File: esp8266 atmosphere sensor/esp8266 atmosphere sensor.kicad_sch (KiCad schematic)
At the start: 23 parts, among them J1 Conn_02x03_Odd_Even, J2 UJ2-MIBH-G-SMT-TR, J3 LUX sensor, J4 bme280, J5 PIR, J6 Analog in, SW1 SW_MEC_5E, U1 ESP-12F, U2 LD1117S33TR_SOT223

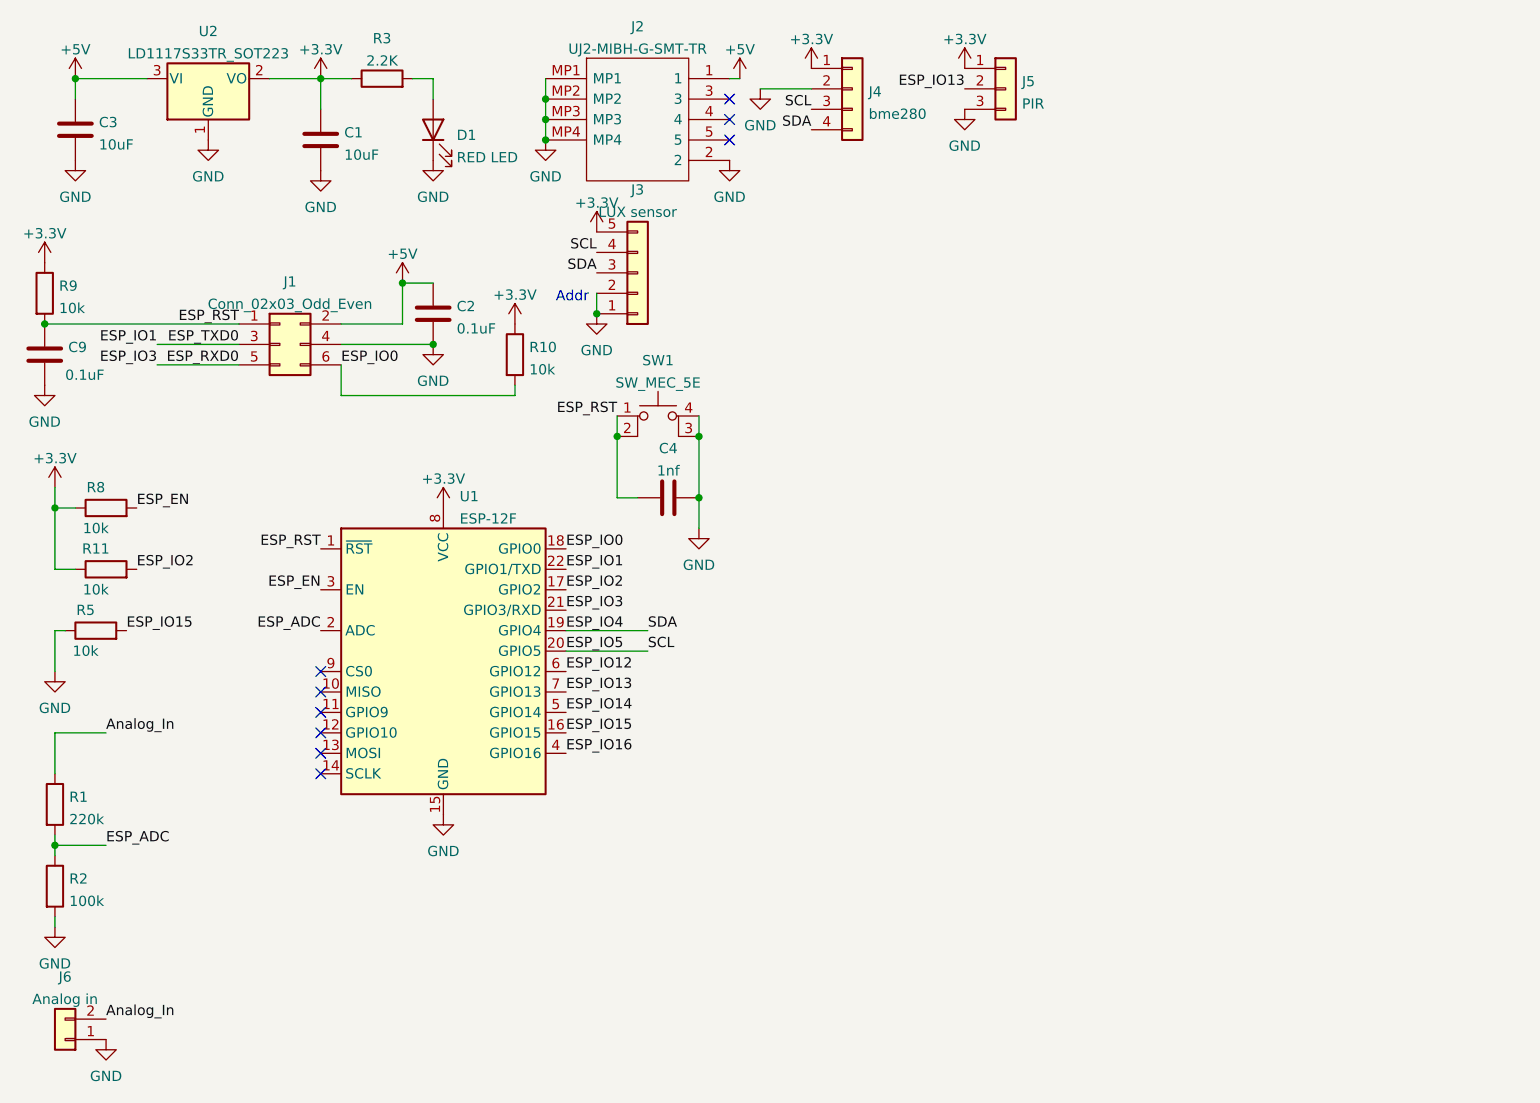
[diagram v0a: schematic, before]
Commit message: added extra i2c and filtered buttons
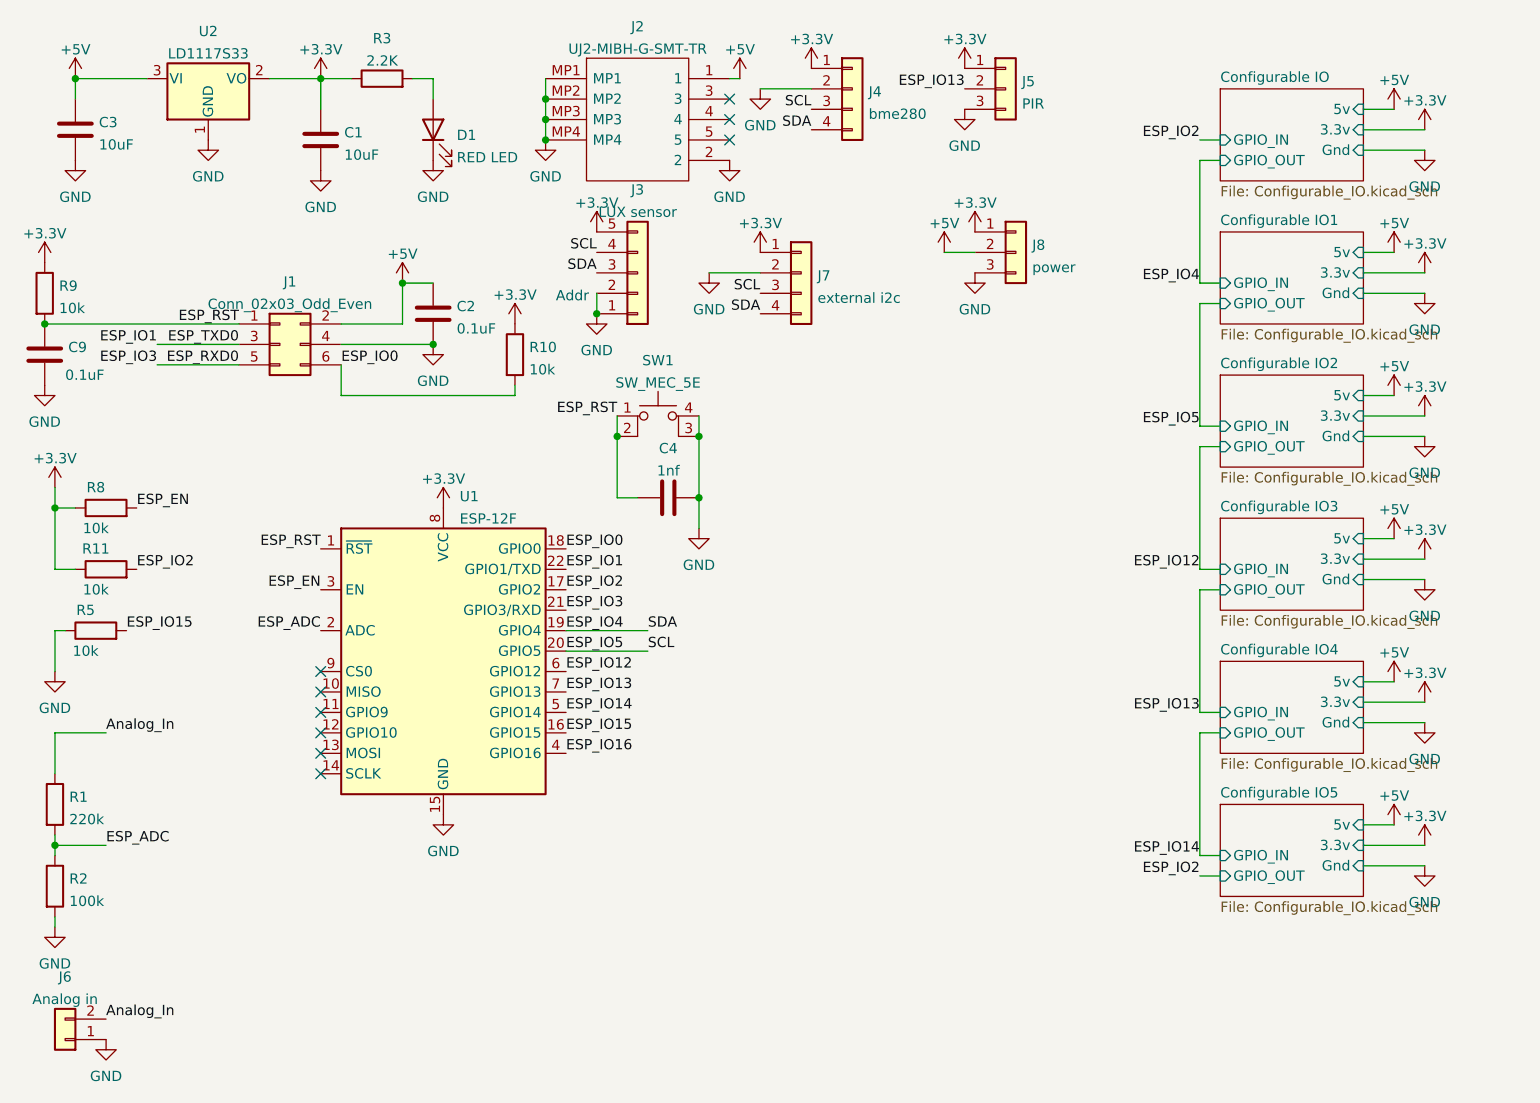
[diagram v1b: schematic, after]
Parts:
- added J7: external i2c, Connector_PinHeader_2.54mm:PinHeader_1x04_P2.54mm_Vertical, symbol Connector_Generic:Conn_01x04
- added J8: power, Connector_PinHeader_2.54mm:PinHeader_1x03_P2.54mm_Vertical, symbol Connector_Generic:Conn_01x03
- U2: value LD1117S33TR_SOT223 -> LD1117S33
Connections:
- net +3V3: now also J7.1 (Pin_1), J8.1 (Pin_1)
- net +5V: now also J8.2 (Pin_2)
- net ESP_IO4: now also J7.4 (Pin_4)
- net ESP_IO5: now also J7.3 (Pin_3)
- net GND: now also J7.2 (Pin_2), J8.3 (Pin_3)
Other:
- added sheet Configurable IO (Configurable_IO.kicad_sch)
- added sheet Configurable IO1 (Configurable_IO.kicad_sch)
- added sheet Configurable IO2 (Configurable_IO.kicad_sch)
- added sheet Configurable IO3 (Configurable_IO.kicad_sch)
- added sheet Configurable IO4 (Configurable_IO.kicad_sch)
- added sheet Configurable IO5 (Configurable_IO.kicad_sch)

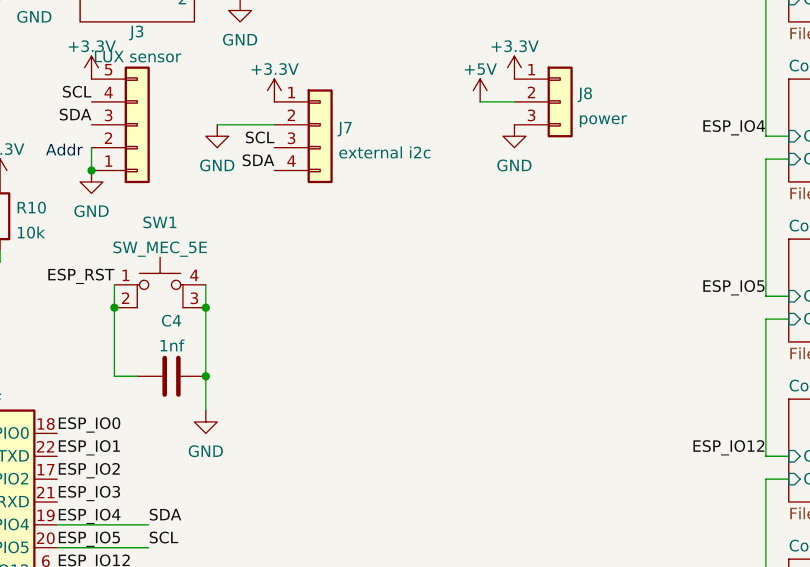
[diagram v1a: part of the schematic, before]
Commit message: tweaked locations for button connectors
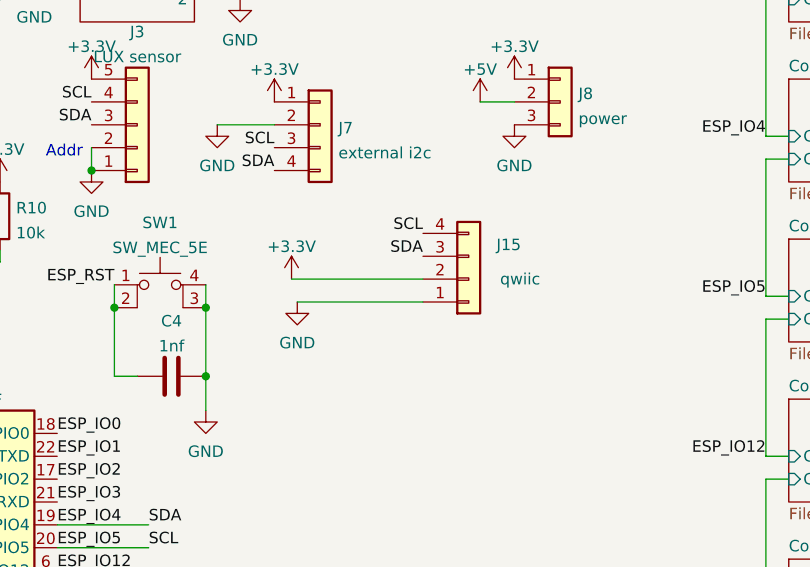
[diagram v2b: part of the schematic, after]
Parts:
- added J15: qwiic, Connector_JST:JST_SH_SM04B-SRSS-TB_1x04-1MP_P1.00mm_Horizontal, symbol Connector_Generic:Conn_01x04
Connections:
- net +3V3: now also J15.2 (Pin_2)
- net ESP_IO4: now also J15.3 (Pin_3)
- net ESP_IO5: now also J15.4 (Pin_4)
- net GND: now also J15.1 (Pin_1)
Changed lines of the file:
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@@
+    (stroke (width 0) (type default) (color 0 0 0 0))
+  )
+  (wire (pts (xy 110.49 66.675) (xy 124.46 66.675))
     (stroke (width 0) (type default) (color 0 0 0 0))
   )
@@
     (stroke (width 0) (type default) (color 0 0 0 0))
   )
+  (wire (pts (xy 109.855 64.135) (xy 124.46 64.135))
+    (stroke (width 0) (type default) (color 0 0 0 0))
+  )
   (wire (pts (xy 33.02 55.88) (xy 43.18 55.88))
     (stroke (width 0) (type default) (color 0 0 0 0))
@@
     (effects (font (size 1.27 1.27)) (justify right bottom))
   )
+  (label "SCL" (at 124.46 59.055 180)
+    (effects (font (size 1.27 1.27)) (justify right bottom))
+  )
   (label "ESP_RST" (at 90.17 64.77 180)
     (effects (font (size 1.27 1.27)) (justify right bottom))
   )
   (label "ESP_IO13" (at 162.56 101.6 180)
+    (effects (font (size 1.27 1.27)) (justify right bottom))
+  )
+  (label "SDA" (at 124.46 61.595 180)
     (effects (font (size 1.27 1.27)) (justify right bottom))
   )
@@
     (pin "1")
   )
+  (symbol (lib_id "power:GND") (at 110.49 66.675 0) (unit 1)
+    (in_bom yes) (on_board yes) (fields_autoplaced)
+    (property "Reference" "#PWR0175" (id 0) (at 110.49 73.025 0)
+      (effects (font (size 1.27 1.27)) hide)
+    )
+    (property "Value" "GND" (id 1) (at 110.49 71.2375 0))
+    (property "Footprint" "" (id 2) (at 110.49 66.675 0)
+      (effects (font (size 1.27 1.27)) hide)
+    )
+    (property "Datasheet" "" (id 3) (at 110.49 66.675 0)
+      (effects (font (size 1.27 1.27)) hide)
+    )
+    (pin "1")
+  )
   (symbol (lib_id "power:+3.3V") (at 53.34 22.86 0) (unit 1)
     (in_bom yes) (on_board yes) (fields_autoplaced)
@@
     )
     (property "Datasheet" "" (id 3) (at 114.3 21.59 0)
+      (effects (font (size 1.27 1.27)) hide)
+    )
+    (pin "1")
+  )
+  (symbol (lib_id "power:+3.3V") (at 109.855 64.135 0) (unit 1)
+    (in_bom yes) (on_board yes) (fields_autoplaced)
+    (property "Reference" "#PWR0176" (id 0) (at 109.855 67.945 0)
+      (effects (font (size 1.27 1.27)) hide)
+    )
+    (property "Value" "+3.3V" (id 1) (at 109.855 60.5305 0))
+    (property "Footprint" "" (id 2) (at 109.855 64.135 0)
+      (effects (font (size 1.27 1.27)) hide)
+    )
+    (property "Datasheet" "" (id 3) (at 109.855 64.135 0)
       (effects (font (size 1.27 1.27)) hide)
     )
@@
     )
     (pin "1")
+  )
+  (symbol (lib_id "Connector_Generic:Conn_01x04") (at 129.54 64.135 0) (mirror x) (unit 1)
+    (in_bom yes) (on_board yes)
+    (property "Reference" "J15" (id 0) (at 133.985 60.325 0))
+    (property "Value" "qwiic" (id 1) (at 135.255 64.135 0))
+    (property "Footprint" "Connector_JST:JST_SH_SM04B-SRSS-TB_1x04-1MP_P1.00mm_Horizontal" (id 2) (at 129.54 64.135 0)
+      (effects (font (size 1.27 1.27)) hide)
+    )
+    (property "Datasheet" "~" (id 3) (at 129.54 64.135 0)
+      (effects (font (size 1.27 1.27)) hide)
+    )
+    (pin "1")
+    (pin "2")
+    (pin "3")
+    (pin "4")
   )
   (symbol (lib_id "Regulator_Linear:LD1117S33TR_SOT223") (at 39.37 22.86 0) (unit 1)
@@
       (reference "#PWR0174") (unit 1) (value "GND") (footprint "")
     )
+    (path "/b367d731-810d-4dbe-aa2e-ab2616fc23ec"
+      (reference "#PWR0175") (unit 1) (value "GND") (footprint "")
+    )
+    (path "/c2fd4927-8431-4c85-b75d-1336c8306cc2"
+      (reference "#PWR0176") (unit 1) (value "+3.3V") (footprint "")
+    )
     (path "/403a5562-9ff8-4886-81c9-a5c5e513807f"
       (reference "C1") (unit 1) (value "10uF") (footprint "Capacitor_SMD:C_1206_3216Metric")
@@
       (reference "J14") (unit 1) (value "Conn_01x03") (footprint "Connector_JST:JST_PH_B3B-PH-SM4-TB_1x03-1MP_P2.00mm_Vertical")
     )
+    (path "/ed10cf49-3728-47fc-ad8f-3d2a7ebae505"
+      (reference "J15") (unit 1) (value "qwiic") (footprint "Connector_JST:JST_SH_SM04B-SRSS-TB_1x04-1MP_P1.00mm_Horizontal")
+    )
     (path "/26048f65-d079-47ec-a354-44fc6c640ac8"
